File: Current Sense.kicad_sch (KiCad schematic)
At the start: 1 part, among them U2 ACS711xLCTR-12AB

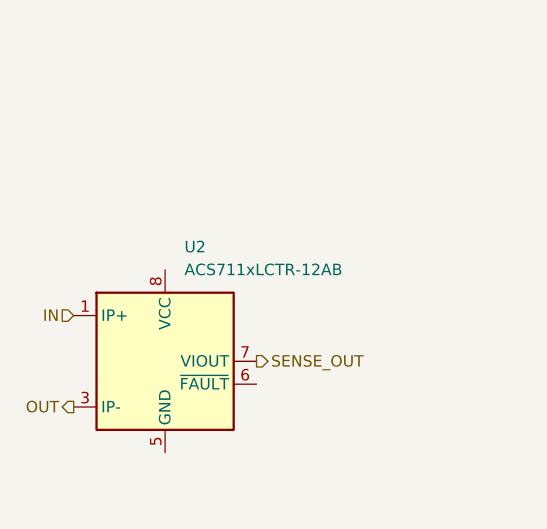
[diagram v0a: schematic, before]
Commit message: add MCU and power circuits
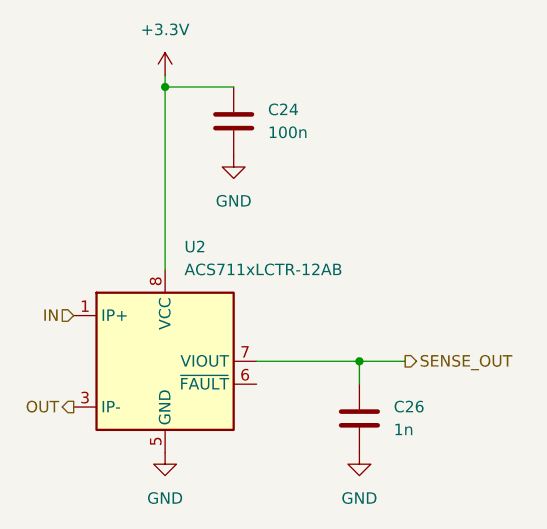
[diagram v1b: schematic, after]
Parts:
- added C24: 100n, Capacitor_SMD:C_0603_1608Metric_Pad1.08x0.95mm_HandSolder, symbol Device:C
- added C26: 1n, Capacitor_SMD:C_0603_1608Metric_Pad1.08x0.95mm_HandSolder, symbol Device:C
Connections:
- net SENSE_OUT: now also C26.1
- net GND: now reaches U2.5 (GND)
- net GND: now also C24.2, C26.2
- net +3.3V: now reaches U2.8 (VCC)
- net +3.3V: now also C24.1
